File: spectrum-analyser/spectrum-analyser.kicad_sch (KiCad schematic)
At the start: 10 parts, among them J1 Conn_Coaxial, J2 Conn_01x02, SW1 SW_SPDT, U1 1.3" OLED, U2 RX5808(V3.3), U4 ESP32-C3_Zero

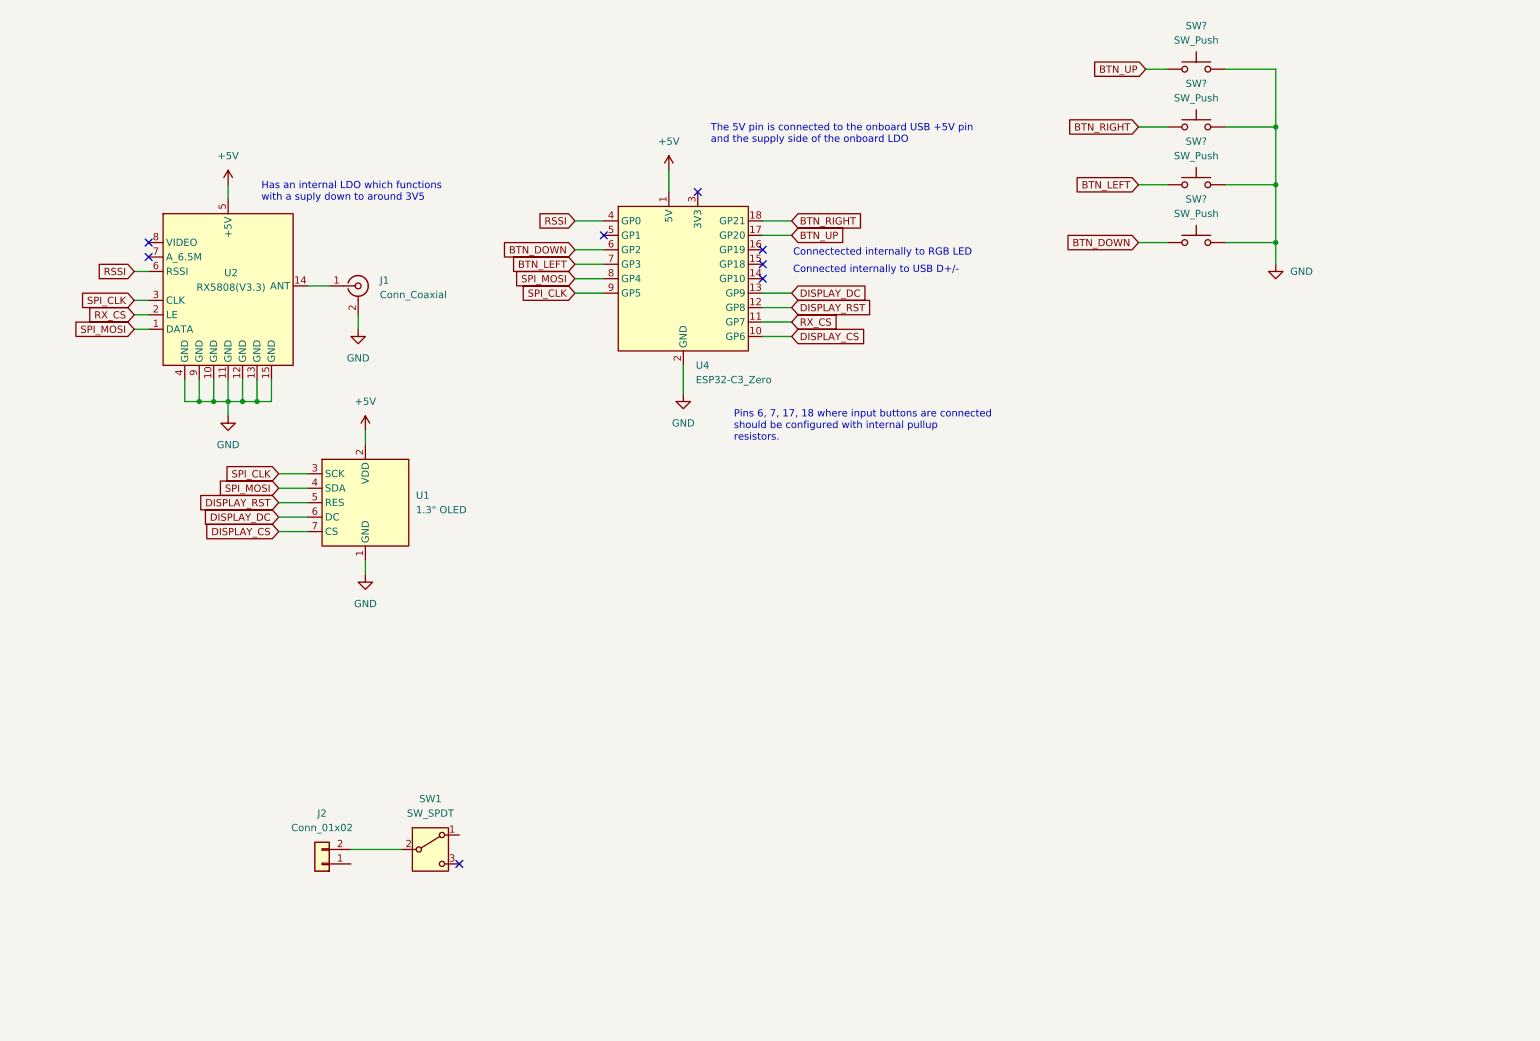
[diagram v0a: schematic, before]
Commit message: Format schematic sheet
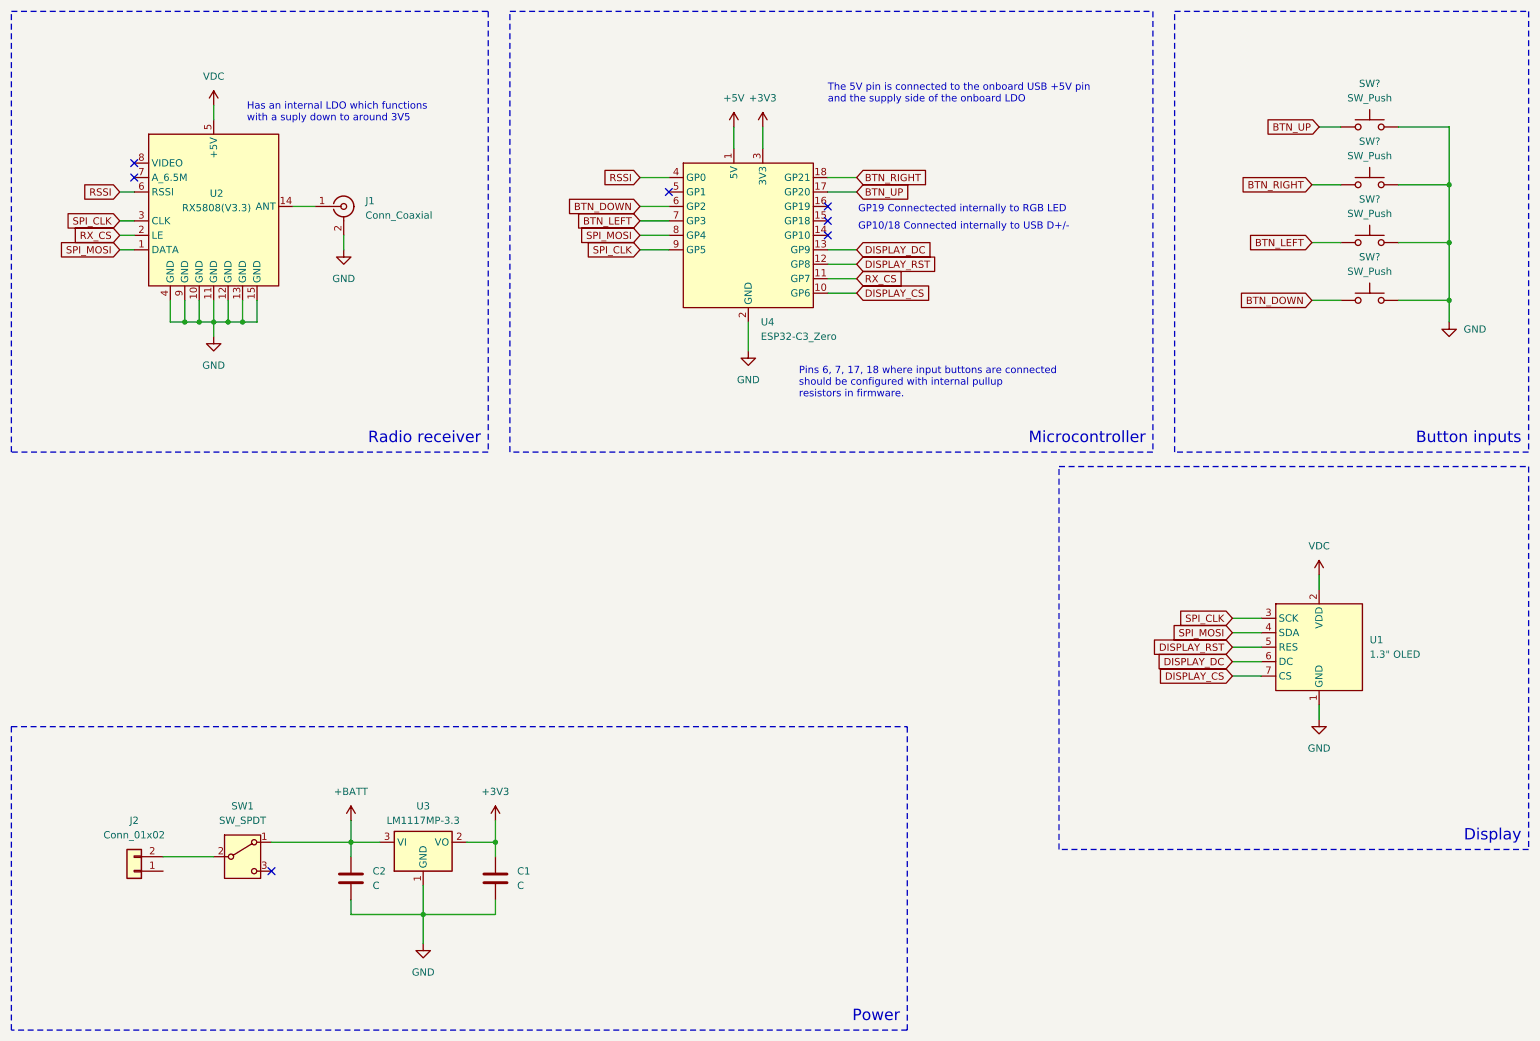
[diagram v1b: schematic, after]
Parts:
- added C1, C2: C, symbol Device:C
- added U3: LM1117MP-3.3, Package_TO_SOT_SMD:SOT-223-3_TabPin2, symbol Regulator_Linear:LM1117MP-3.3
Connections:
- net +5V: no longer U1.2 (VDD), U2.5 (+5V)
- net GND: now also C1.2, C2.2, U3.1 (GND)
- net +BATT: now reaches SW1.1 (A)
- net +BATT: now also C2.1, U3.3 (VI)
- net +3V3: now reaches U4.3 (3V3)
- net +3V3: now also C1.1, U3.2 (VO)
- new net VDC: U1.2 (VDD), U2.5 (+5V)
- no-connect marks 8 -> 7
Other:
- note added: "Button inputs"
- note added: "Display"
- note added: "GP10/18 Connected internally to USB D+/-"
- note added: "GP19 Connectected internally to RGB LED"
- note added: "Microcontroller"
- note added: "Pins 6, 7, 17, 18 where input buttons are connected should be configured with internal pullup resistors in firmware."
- note added: "Power"
- note added: "Radio receiver"
- note removed: "Connectected internally to RGB LED"
- note removed: "Connected internally to USB D+/-"
- note removed: "Pins 6, 7, 17, 18 where input buttons are connected should be configured with internal pullup resistors."
- moved on the sheet: J1, J2, SW1, SW?, U1, U2, U4

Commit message: Add power and battery charge management to schematic
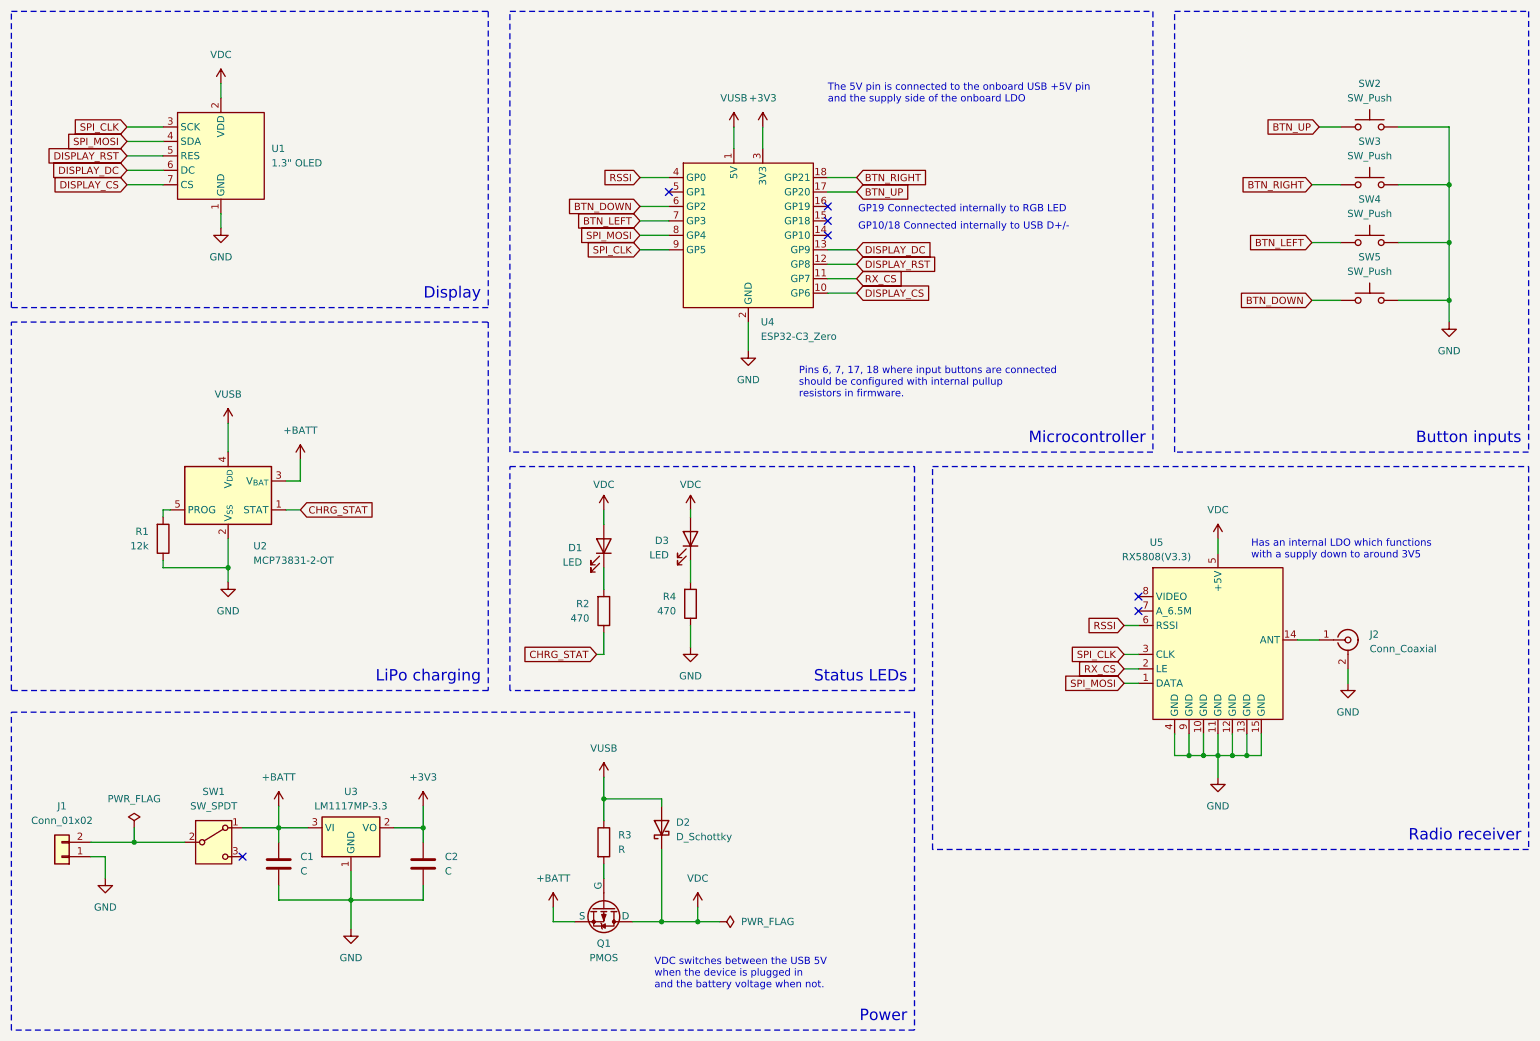
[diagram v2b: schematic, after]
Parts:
- added D1, D3: LED, symbol Device:LED
- added D2: D_Schottky, symbol Device:D_Schottky
- added Q1: PMOS, symbol Simulation_SPICE:PMOS
- added R1: 12k, symbol Device:R
- added R2, R4: 470, symbol Device:R
- added R3: R, symbol Device:R
- added U2: MCP73831-2-OT, Package_TO_SOT_SMD:SOT-23-5, symbol Battery_Management:MCP73831-2-OT
- gave numbers to parts that had none: 4
- renumbered C2 to C1, C1 to C2, J2 to J1, J1 to J2, U2 to U5
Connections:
- net +BATT: now also Q1.3 (S), U2.3 (V_{BAT})
- net GND: now also J1.1 (Pin_1), R1.1, R4.1, U2.2 (V_{SS})
- net VDC: now also D1.2 (A), D2.1 (K), D3.2 (A), Q1.1 (D)
- net +5V renamed VUSB
- net VUSB: now also D2.2 (A), R3.1, U2.4 (V_{DD})
- new net: R1.2, U2.5 (PROG)
- new net: Q1.2 (G), R3.2
- new net: D1.1 (K), R2.2
- new net: D3.1 (K), R4.2
- new net CHRG_STAT: R2.1, U2.1 (STAT)
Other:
- note added: "Has an internal LDO which functions with a supply down to around 3V5"
- note added: "LiPo charging"
- note added: "Status LEDs"
- note added: "VDC switches between the USB 5V when the device is plugged in and the battery voltage when not."
- note removed: "Has an internal LDO which functions with a suply down to around 3V5"
- moved on the sheet: C1, C2, J1, J2, SW1, U1, U3, U5

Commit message: Add battery protection and modify power delivery
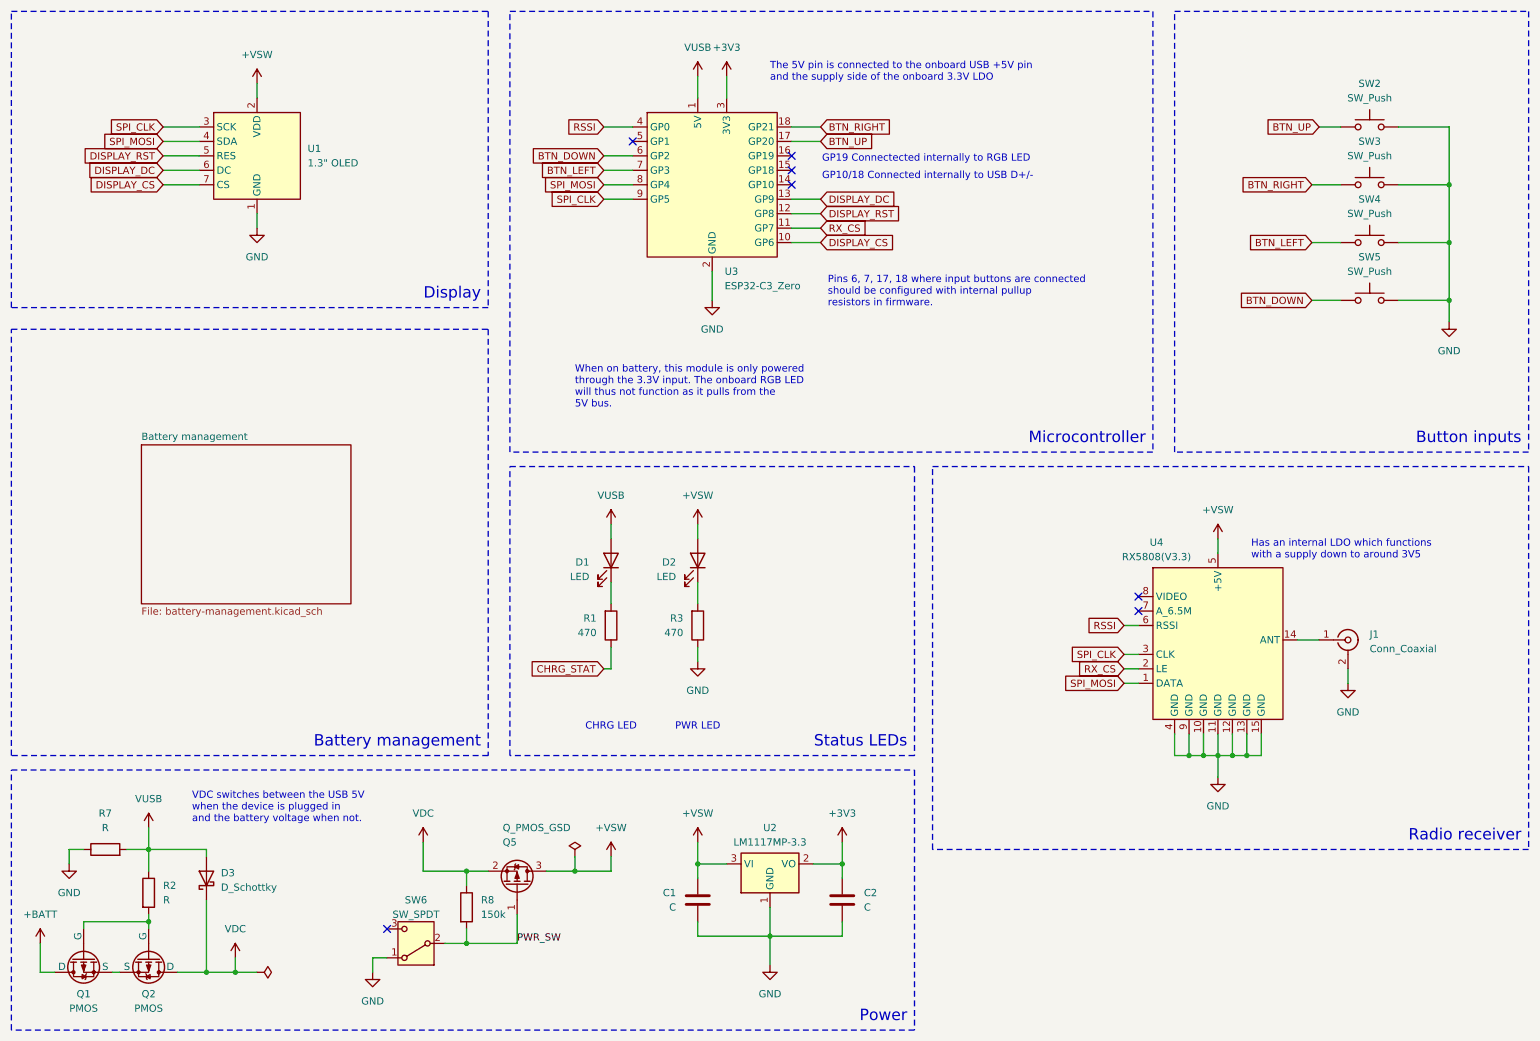
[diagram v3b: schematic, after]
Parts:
- removed J1: Conn_01x02, symbol Connector_Generic:Conn_01x02
- removed R1: 12k, symbol Device:R
- removed SW1: SW_SPDT, symbol Switch:SW_SPDT
- removed U2: MCP73831-2-OT, Package_TO_SOT_SMD:SOT-23-5, symbol Battery_Management:MCP73831-2-OT
- added Q1: PMOS, symbol Simulation_SPICE:PMOS
- added Q5: Q_PMOS_GSD, Package_TO_SOT_SMD:SOT-23, symbol Device:Q_PMOS_GSD
- added R7: R, symbol Device:R
- added R8: 150k, Resistor_SMD:R_0603_1608Metric, symbol Device:R
- added SW6: SW_SPDT, thanassis_foot:SW_SPDT_TEC_1825232-1, symbol Switch:SW_SPDT
- renumbered D3 to D2, D2 to D3, J2 to J1, Q1 to Q2, R2 to R1, R3 to R2, R4 to R3, U3 to U2, U4 to U3, U5 to U4
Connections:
- net +BATT: now also Q1.1 (D); no longer C1.1, Q2.3 (S), U2.3 (VI)
- net GND: now also R7.1, SW6.1 (A)
- net VDC: now also Q5.2 (S), R8.1; no longer D1.2 (A), D2.2 (A), U1.2 (VDD), U4.5 (+5V)
- net VUSB: now also D1.2 (A), R7.2
- net at Q2.2 (G), R2.2: now also Q1.2 (G)
- new net: Q1.3 (S), Q2.3 (S)
- new net +VSW: C1.1, D2.2 (A), Q5.3 (D), U1.2 (VDD), U2.3 (VI), U4.5 (+5V)
- new net PWR_SW: Q5.1 (G), R8.2, SW6.2 (B)
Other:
- added sheet Battery management (battery-management.kicad_sch)
- note added: "Battery management"
- note added: "CHRG LED"
- note added: "PWR LED"
- note added: "The 5V pin is connected to the onboard USB +5V pin and the supply side of the onboard 3.3V LDO"
- note added: "When on battery, this module is only powered through the 3.3V input. The onboard RGB LED will thus not function as it pulls from the 5V bus."
- note removed: "LiPo charging"
- note removed: "The 5V pin is connected to the onboard USB +5V pin and the supply side of the onboard LDO"
- moved on the sheet: C1, C2, D1, D2, D3, Q2, R1, R2, R3, U1, U2, U3
